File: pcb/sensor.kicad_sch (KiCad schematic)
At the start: 13 parts, among them U2 pmw3360-t2qu

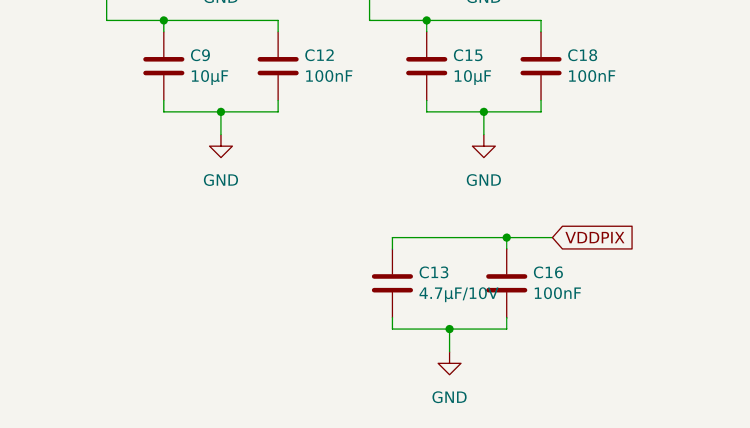
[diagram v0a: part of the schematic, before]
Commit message: cleaned up symbols in schematics a bit
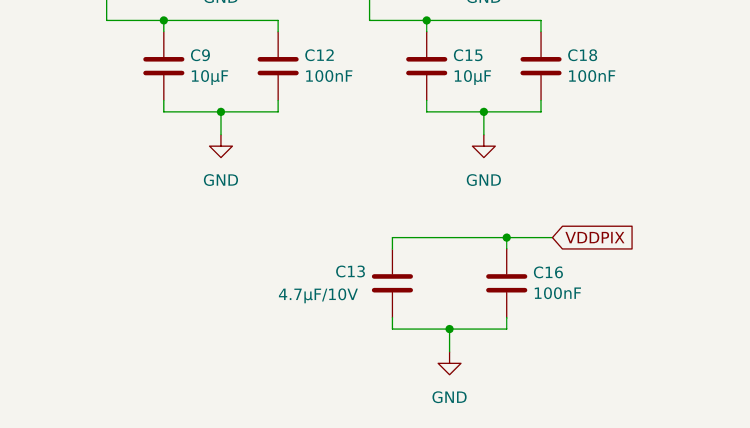
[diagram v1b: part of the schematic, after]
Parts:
- U2: footprint (none) -> mouse:pmw3360-t2qu
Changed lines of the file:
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@@
     (property "Reference" "U2" (id 0) (at 87.63 96.52 0))
     (property "Value" "pmw3360-t2qu" (id 1) (at 100.33 96.52 0))
-    (property "Footprint" "" (id 2) (at 93.98 93.98 0)
+    (property "Footprint" "mouse:pmw3360-t2qu" (id 2) (at 93.98 93.98 0)
       (effects (font (size 1.27 1.27)) hide)
     )
@@
   (symbol (lib_id "Device:C") (at 210.82 127 0) (unit 1)
     (in_bom yes) (on_board yes)
-    (property "Reference" "C13" (id 0) (at 213.741 125.8316 0)
-      (effects (font (size 1.27 1.27)) (justify left))
-    )
-    (property "Value" "4.7μF/10V" (id 1) (at 213.741 128.143 0)
-      (effects (font (size 1.27 1.27)) (justify left))
-    )
+    (property "Reference" "C13" (id 0) (at 204.47 125.73 0)
+      (effects (font (size 1.27 1.27)) (justify left))
+    )
+    (property "Value" "4.7μF/10V" (id 1) (at 198.12 128.27 0)
+      (effects (font (size 1.27 1.27)) (justify left))
+    )

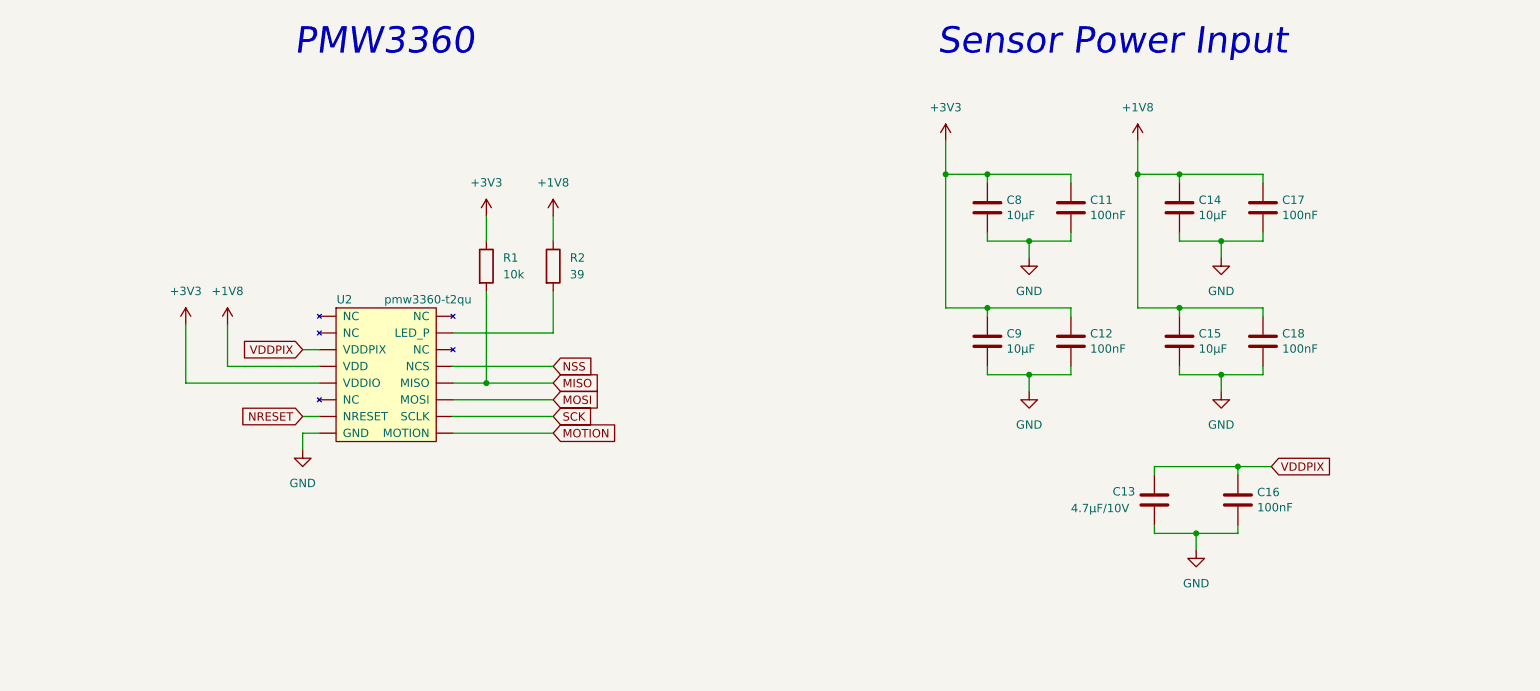
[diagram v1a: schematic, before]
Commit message: - split schematic to lists - changed global ports to local - assigned footprints to majority of schematic parts
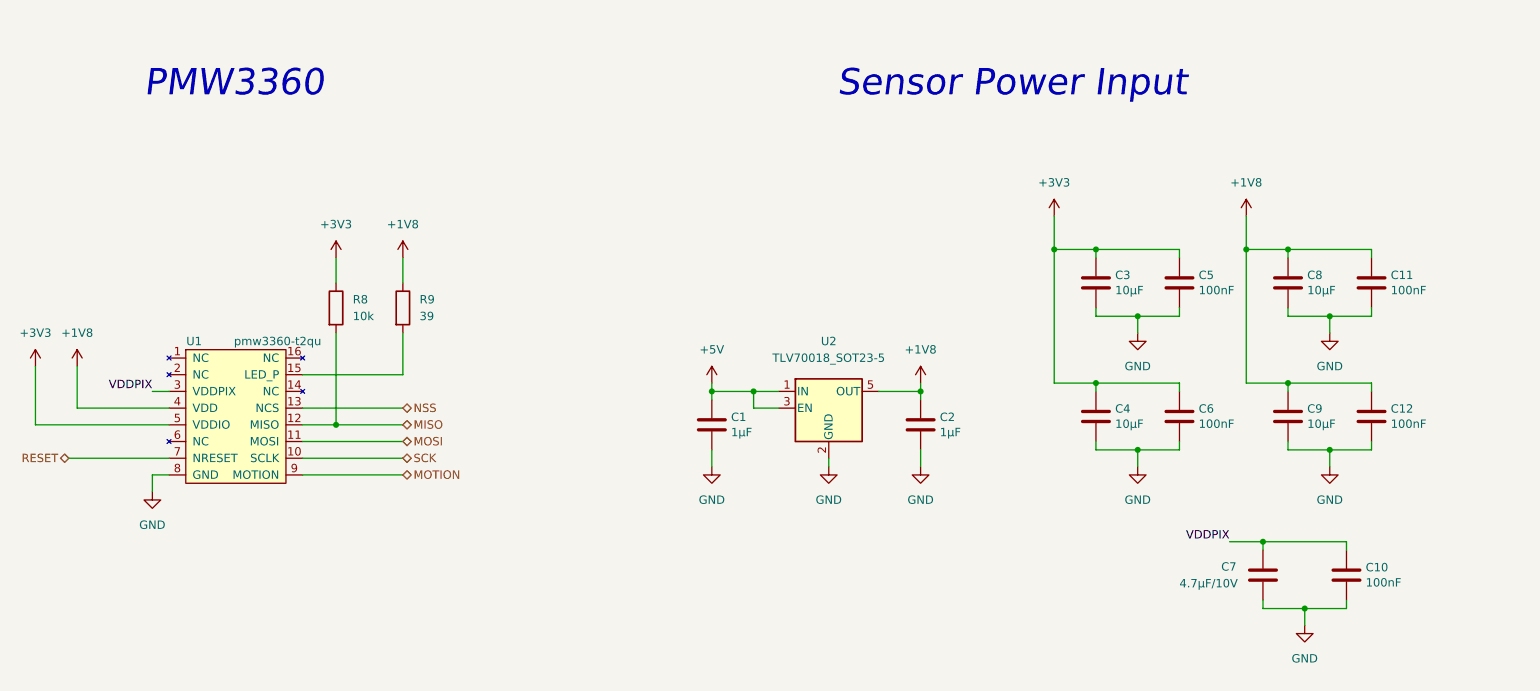
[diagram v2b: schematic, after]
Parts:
- added C1, C2: 1μF, Capacitor_SMD:C_0603_1608Metric, symbol Device:C
- added U2: TLV70018_SOT23-5, Package_TO_SOT_SMD:SOT-23-5, symbol Regulator_Linear:TLV70018_SOT23-5
- C10: renamed from C16; footprint (none) -> Capacitor_SMD:C_0603_1608Metric
- C11: renamed from C17; footprint (none) -> Capacitor_SMD:C_0603_1608Metric
- C12: renamed from C18; footprint (none) -> Capacitor_SMD:C_0603_1608Metric
- C3: renamed from C8; footprint (none) -> Capacitor_SMD:C_0603_1608Metric
- C4: renamed from C9; footprint (none) -> Capacitor_SMD:C_0603_1608Metric
- C5: renamed from C11; footprint (none) -> Capacitor_SMD:C_0603_1608Metric
- C6: renamed from C12; footprint (none) -> Capacitor_SMD:C_0603_1608Metric
- C7: renamed from C13; footprint (none) -> Capacitor_SMD:C_0603_1608Metric
- C8: renamed from C14; footprint (none) -> Capacitor_SMD:C_0603_1608Metric
- C9: renamed from C15; footprint (none) -> Capacitor_SMD:C_0603_1608Metric
- R8: renamed from R1; footprint (none) -> Resistor_SMD:R_0603_1608Metric
- R9: renamed from R2; footprint (none) -> Resistor_SMD:R_0603_1608Metric
- renumbered U2 to U1
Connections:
- net +1V8: now also U1.4 (VDD), C2.1, U2.5 (OUT); no longer U1.~ (VDDPIX)
- net +3V3: now also U1.5 (VDDIO); no longer U1.~ (VDDPIX)
- net GND: now also U1.8 (GND), C1.2, C2.2, U2.2 (GND); no longer U1.~ (VDDPIX)
- net MISO: now also U1.12 (MISO); no longer U1.~ (VDDPIX)
- net MOSI: now also U1.11 (MOSI); no longer U1.~ (VDDPIX)
- net MOTION: now also U1.9 (MOTION); no longer U1.~ (VDDPIX)
- net NSS: now also U1.13 (NCS); no longer U1.~ (VDDPIX)
- net SCK: now also U1.10 (SCLK); no longer U1.~ (VDDPIX)
- net VDDPIX: now also U1.3 (VDDPIX); no longer U1.~ (VDDPIX)
- net at R9.2: now also U1.15 (LED_P); no longer U1.~ (VDDPIX)
- removed net NRESET: U1.~ (VDDPIX)
- new net +5V: C1.1, U2.1 (IN), U2.3 (EN)
- new net RESET: U1.7 (NRESET)
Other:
- moved on the sheet: C10, C11, C12, C3, C4, C5, C6, C7, C8, C9, R8, R9

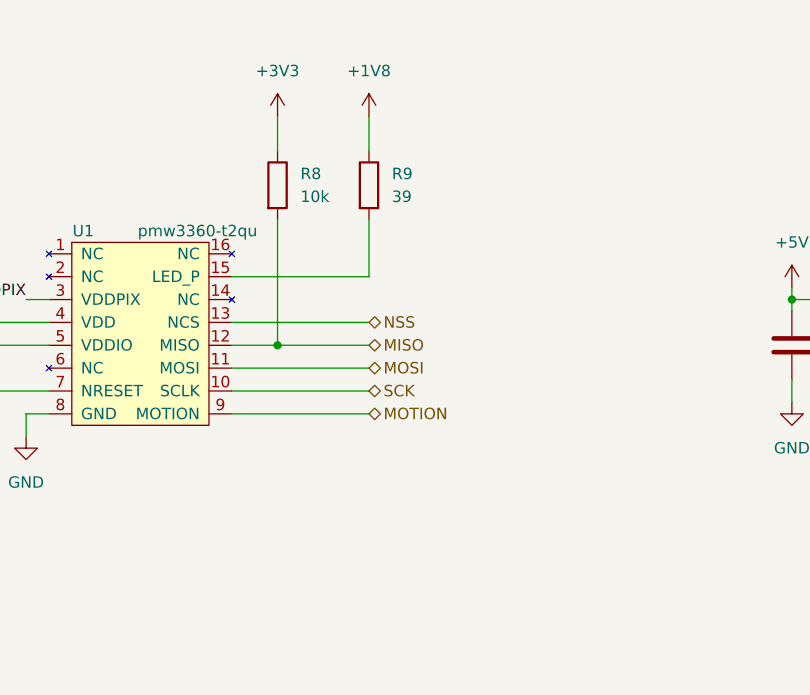
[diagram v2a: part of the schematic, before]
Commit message: - added debouncing to buttons - assigned some footprints - added expansion and inspection pin headers
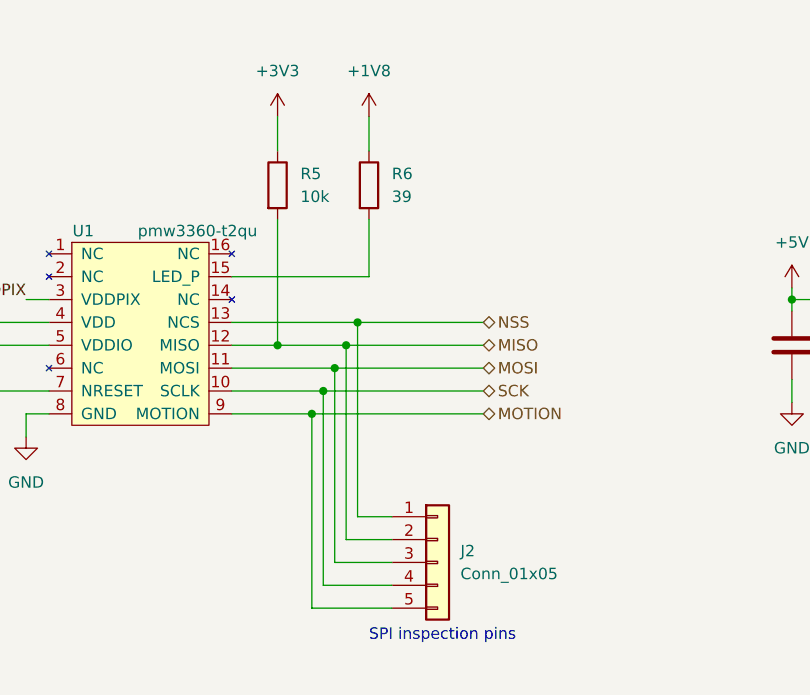
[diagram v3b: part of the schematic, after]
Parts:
- added J2: Conn_01x05, Connector_PinSocket_2.54mm:PinSocket_1x05_P2.54mm_Vertical, symbol Connector_Generic:Conn_01x05
- renumbered R8 to R5, R9 to R6
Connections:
- net MISO: now also J2.2 (Pin_2)
- net MOSI: now also J2.3 (Pin_3)
- net MOTION: now also J2.5 (Pin_5)
- net NSS: now also J2.1 (Pin_1)
- net SCK: now also J2.4 (Pin_4)
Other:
- note added: "SPI inspection pins"

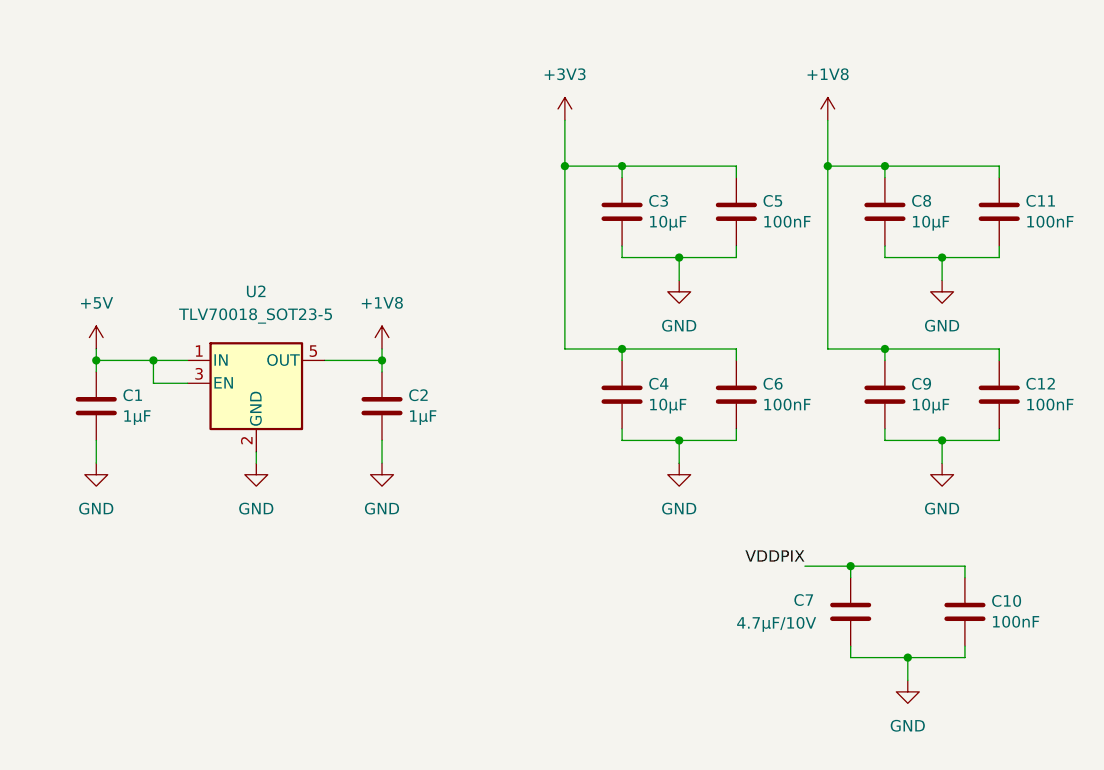
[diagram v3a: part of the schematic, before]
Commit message: added LCSC part numbers and assigned footprints
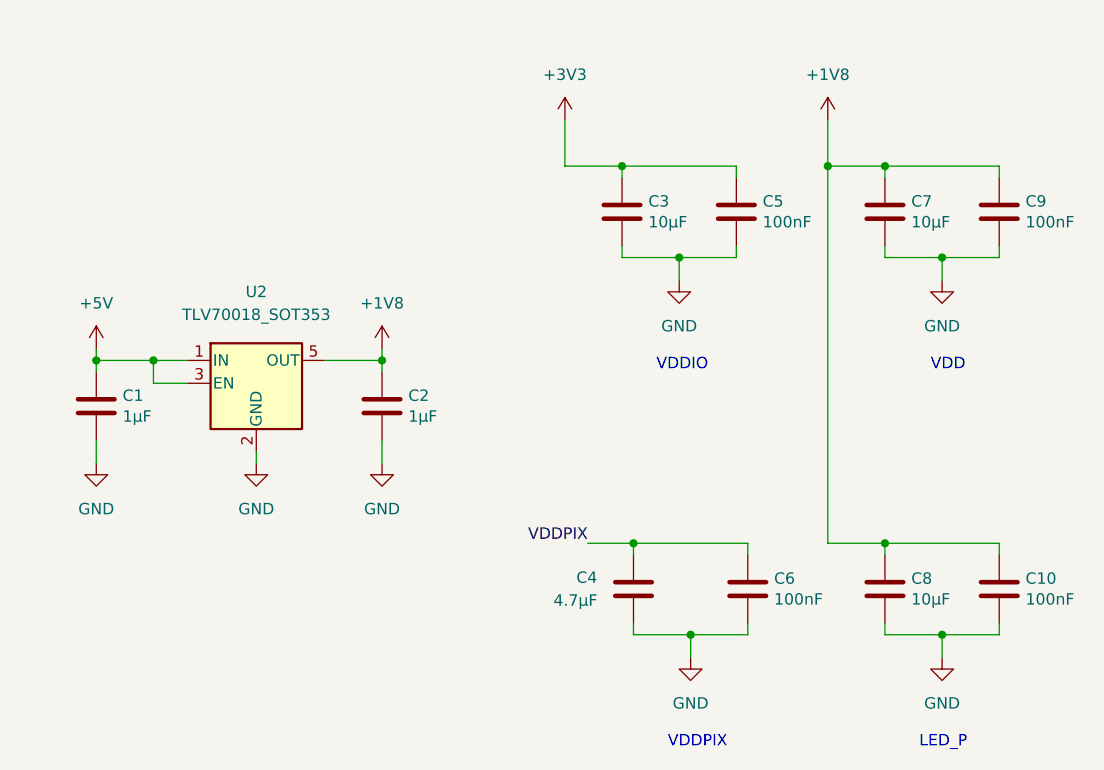
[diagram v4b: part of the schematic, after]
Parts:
- removed C4: 10μF, Capacitor_SMD:C_0603_1608Metric, symbol Device:C
- removed C6: 100nF, Capacitor_SMD:C_0603_1608Metric, symbol Device:C
- removed U2: TLV70018_SOT23-5, Package_TO_SOT_SMD:SOT-23-5, symbol Regulator_Linear:TLV70018_SOT23-5
- added U2: TLV70018_SOT353, Package_TO_SOT_SMD:SOT-353_SC-70-5, symbol Regulator_Linear:TLV70018_SOT353
- C1, C2: LCSC (none) -> C15849
- C10: renamed from C12; LCSC (none) -> C14663
- C3: LCSC (none) -> C19702
- C4: renamed from C7; value 4.7μF/10V -> 4.7μF; LCSC (none) -> C19666
- C5: LCSC (none) -> C14663
- C6: renamed from C10; LCSC (none) -> C14663
- C7: renamed from C8; LCSC (none) -> C19702
- C8: renamed from C9; LCSC (none) -> C19702
- C9: renamed from C11; LCSC (none) -> C14663
- R5: LCSC (none) -> C25804
- R6: LCSC (none) -> C227890
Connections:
- net +1V8: now also U2.5 (OUT)
- net +5V: now also U2.1 (IN), U2.3 (EN)
- net GND: now also U2.2 (GND)
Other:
- note added: "LED_P"
- note added: "VDD"
- note added: "VDDIO"
- note added: "VDDPIX"
- moved on the sheet: C10, C4, C6, C8

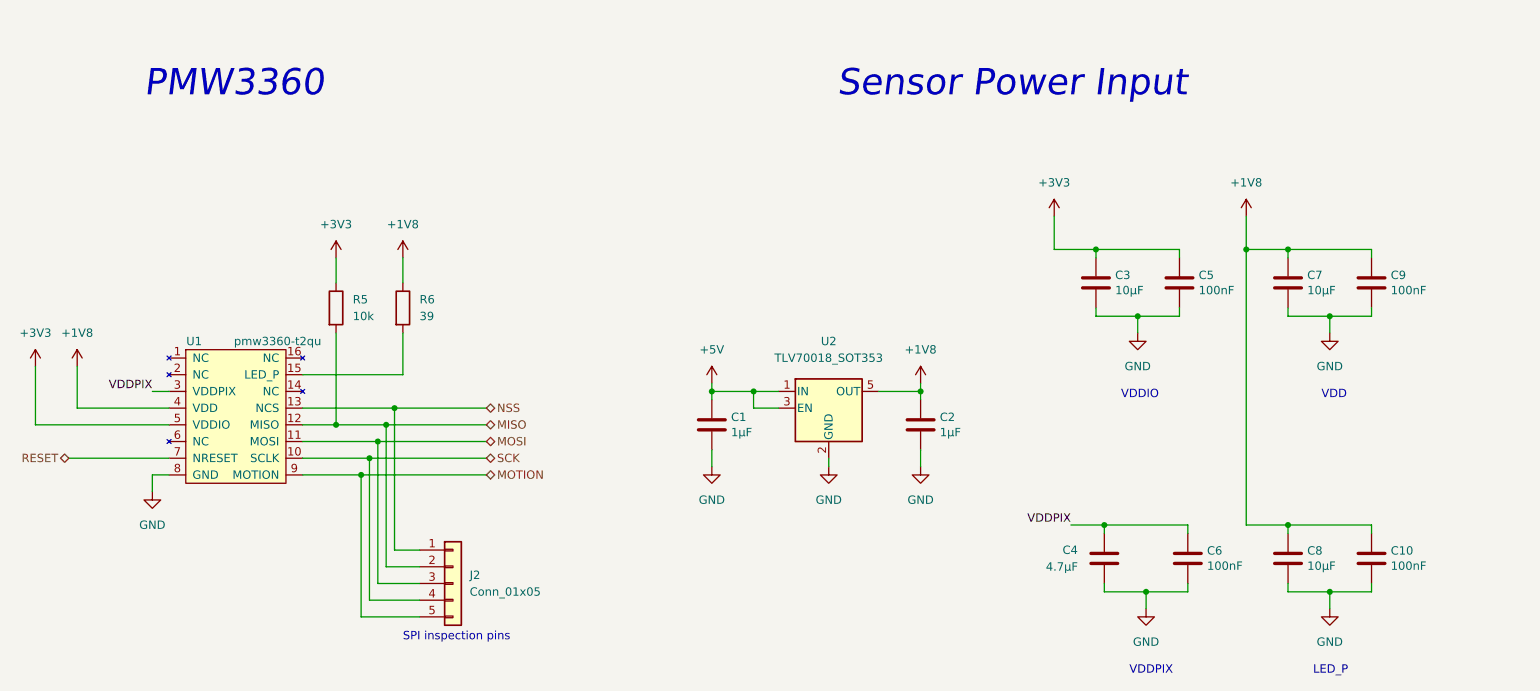
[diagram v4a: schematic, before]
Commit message: - added status leds - changed some lcsc components
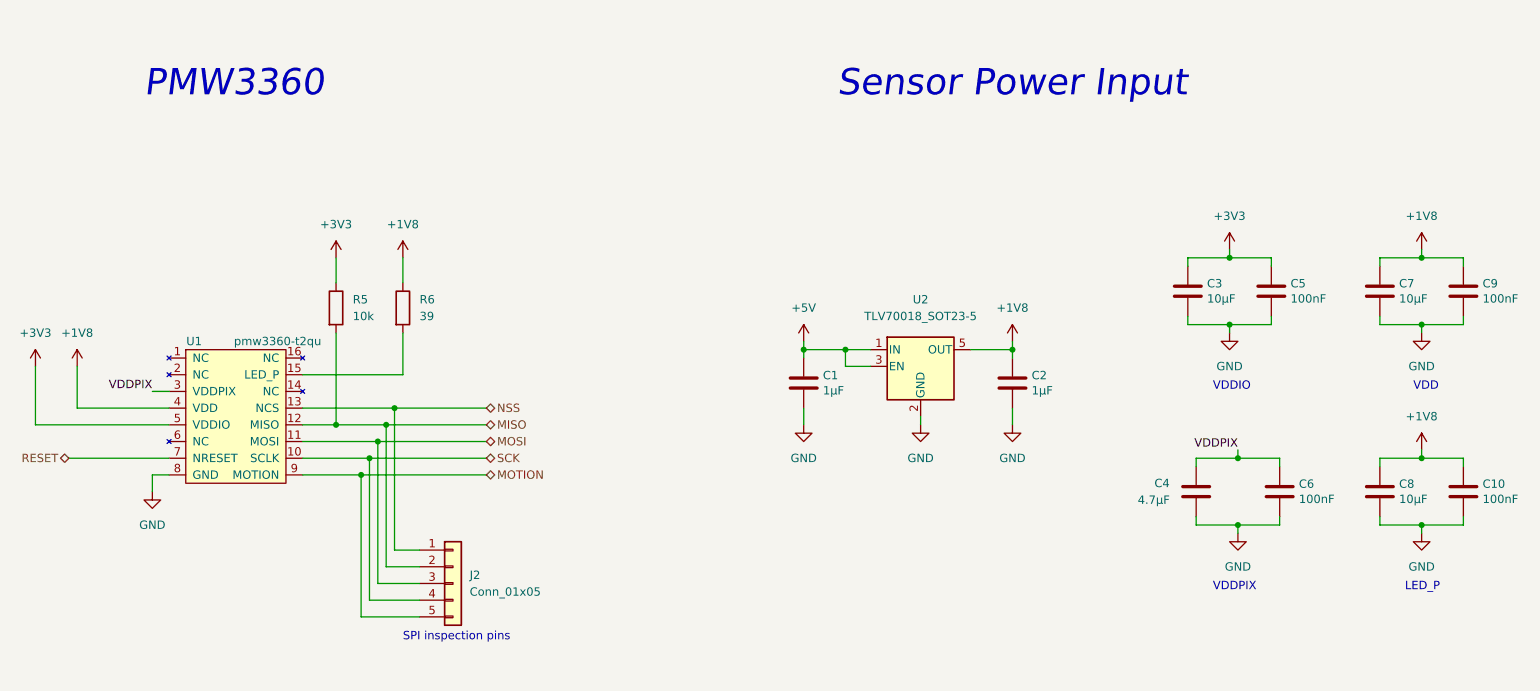
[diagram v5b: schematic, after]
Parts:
- removed U2: TLV70018_SOT353, Package_TO_SOT_SMD:SOT-353_SC-70-5, symbol Regulator_Linear:TLV70018_SOT353
- added U2: TLV70018_SOT23-5, Package_TO_SOT_SMD:SOT-23-5, symbol Regulator_Linear:TLV70018_SOT23-5
- J2: footprint Connector_PinSocket_2.54mm:PinSocket_1x05_P2.54mm_Vertical -> Connector_PinHeader_2.54mm:PinHeader_1x05_P2.54mm_Vertical
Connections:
- net +1V8: now also U2.5 (OUT)
- net +5V: now also U2.1 (IN), U2.3 (EN)
- net GND: now also U2.2 (GND)
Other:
- moved on the sheet: C1, C10, C2, C3, C4, C5, C6, C7, C8, C9
